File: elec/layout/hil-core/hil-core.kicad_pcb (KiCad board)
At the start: 4 copper layers, 81 parts, among them U4 10µH ±20%

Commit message: update core layout
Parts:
- added C30: 10µF ±10% 10V X5R, atopile:C0603-bd72f6, F.Cu at (175.9, 68.6)
- added C31: 10µF ±10% 10V X5R, atopile:C0603-bd72f6, F.Cu at (167.1, 55.7)
- added C32: 100nF ±10% 16V X7R, atopile:C0402-b3ef17, F.Cu at (177.6, 60.1)
- added C33: 100nF ±10% 16V X7R, atopile:C0402-b3ef17, F.Cu at (171.4, 68.7)
- added C34: 100nF ±10% 16V X7R, atopile:C0402-b3ef17, F.Cu at (177.5, 58.1)
- added C35: 100nF ±10% 16V X7R, atopile:C0402-b3ef17, F.Cu at (170.4, 68.7)
- added C36: 100nF ±10% 16V X7R, atopile:C0402-b3ef17, F.Cu at (173.1, 68.5)
- added C37: 100nF ±10% 16V X7R, atopile:C0402-b3ef17, F.Cu at (177.6, 63.3)
- added C38: 20pF ±5% 50V C0G, atopile:C0402-b3ef17, F.Cu at (168.5, 56.1)
- added C39: 20pF ±5% 50V C0G, atopile:C0402-b3ef17, F.Cu at (171.3, 53.9)
- added C40: 10µF ±10% 10V X5R, atopile:C0603-bd72f6, F.Cu at (166.9, 73.4)
- added C41: 10µF ±10% 10V X5R, atopile:C0603-bd72f6, F.Cu at (174.3, 71.7)
- added C42: 10µF ±10% 10V X5R, atopile:C0603-bd72f6, F.Cu at (174.4, 74.5)
- added C43: 10µF ±10% 10V X5R, atopile:C0603-bd72f6, F.Cu at (175.8, 71.7)
- added C44: 10µF ±10% 10V X5R, atopile:C0603-bd72f6, F.Cu at (172.9, 71.8)
- added C45: 10µF ±10% 10V X5R, atopile:C0603-bd72f6, F.Cu at (173.0, 74.5)
- added D10: , atopile:SOT-143_L2.9-W1.3-P1.92-LS2.3-BR-44397f, F.Cu at (167.2, 65.7)
- added D11: , atopile:SOT-143_L2.9-W1.3-P1.92-LS2.3-BR-44397f, F.Cu at (167.2, 69.0)
- added D12: , atopile:SOT-143_L2.9-W1.3-P1.92-LS2.3-BR-44397f, F.Cu at (175.3, 56.1)
- added D8: , atopile:SOT-143_L2.9-W1.3-P1.92-LS2.3-BR-44397f, F.Cu at (167.2, 59.2)
- added D9: , atopile:SOT-143_L2.9-W1.3-P1.92-LS2.3-BR-44397f, F.Cu at (167.2, 62.4)
- added R25: 33kΩ ±1% 62.5mW, atopile:R0402-56259e, F.Cu at (177.8, 62.3)
- added R26: 33kΩ ±1% 62.5mW, atopile:R0402-56259e, F.Cu at (177.8, 64.3)
- added R27: 12kΩ ±1% 62.5mW, atopile:R0402-56259e, F.Cu at (169.9, 59.0)
- added R28: 33kΩ ±1% 62.5mW, atopile:R0402-56259e, F.Cu at (177.8, 61.3)
- added R29: 33kΩ ±1% 62.5mW, atopile:R0402-56259e, F.Cu at (177.8, 59.1)
- added R30: 15kΩ ±1% 62.5mW, atopile:R0402-56259e, F.Cu at (169.1, 75.9)
- added R31: 5.1kΩ ±1% 62.5mW, atopile:R0402-56259e, F.Cu at (130.0, 56.4)
- added R32: 5.1kΩ ±1% 62.5mW, atopile:R0402-56259e, F.Cu at (130.1, 59.9)
- added U14: , atopile:SQFN-36_L6.0-W6.0-P0.50-BL-EP-5817ac, F.Cu at (172.7, 63.3)
- added U15: , atopile:SOT-23-6_L2.9-W1.6-P0.95-LS2.8-BR-bfc73b, F.Cu at (170.0, 73.7)
- added X1: , atopile:CRYSTAL-SMD_4P-L3.2-W2.5-BL-1-d85bc6, F.Cu at (171.5, 56.2)
- moved C26 8.13 mm to (163.2, 61.3)
- moved C27 8.13 mm to (163.2, 60.3)
- moved C28 8.13 mm to (163.2, 63.5)
- moved C29 8.13 mm to (163.2, 62.5)
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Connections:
- net A7 renamed line-4
- net A8 renamed usbpd.usb_connector-A8
- net DP1 renamed line-6
- net SBU1 renamed usb_connector.connector-A8
- net controller.cm5-pins[53] renamed pins[53]
- net controller.cm5-pins[89] renamed controller.cm5-pins[87]
- net controller.cm5-pins[89]-1 renamed pins[89]
- net pins[40] renamed controller.cm5.hdi_b-pins[40]
- net pins[87] renamed controller.cm5-pins[87]-1
- net usb_connector-A10 renamed A10
- net usb_connector-A11 renamed A11
- net usb_connector-B2 renamed B2
- net usb_connector-B3 renamed B3
- net usb_connector-B8 renamed B8
- net usb_connector-SSRXN1 renamed usb_connector.connector-B10
- net usb_connector-SSRXP1 renamed usb_connector.connector-B11
- net usb_connector-SSTXN1 renamed usb_connector.connector-A3
- net usb_connector-SSTXP1 renamed usb_connector.connector-A2
- net usb_uart-line renamed line-15
- net usb_uart-line-1 renamed line-10
- net usb_uart-line-2 renamed line-9
- net usb_uart-line-4 renamed line-8
- net usb_uart-line-8 renamed line-14
- net usbpd.usb_connector-A10 renamed SSRXN2
- net usbpd.usb_connector-A11 renamed SSRXP2
- net usbpd.usb_connector-B2 renamed SSTXP2
- net usbpd.usb_connector-B3 renamed SSTXN2
- net usbpd.usb_connector-B8 renamed SBU2
- net usbpd.usb_connector-SSRXN1 renamed usbpd.usb_connector-B10
- net usbpd.usb_connector-SSRXP1 renamed usbpd.usb_connector-B11
- net usbpd.usb_connector-SSTXN1 renamed usbpd.usb_connector-A3
- net usbpd.usb_connector-SSTXP1 renamed usbpd.usb_connector-A2
- C1 pad 2: gnd -> gnd-1
- C10 pad 1: hv-4 -> hv-2
- C10 pad 2: gnd -> gnd-1
- C11 pad 1: hv-4 -> hv-2
- C11 pad 2: gnd -> gnd-1
- C12 pad 1: hv-6 -> hv-9
- C12 pad 2: gnd -> gnd-1
- C15 pad 1: hv-4 -> hv-2
- C15 pad 2: gnd -> gnd-1
- C16 pad 1: hv-3 -> hv-5
- C16 pad 2: gnd -> gnd-1
- C17 pad 1: hv-5 -> hv-4
- C17 pad 2: gnd -> gnd-1
- C18 pad 1: hv-5 -> hv-4
- C18 pad 2: gnd -> gnd-1
- C19 pad 2: gnd -> gnd-1
- C2 pad 1: hv-2 -> hv
- C2 pad 2: gnd -> gnd-1
- C20 pad 1: hv-6 -> hv-9
- C20 pad 2: gnd -> gnd-1
- C21 pad 1: hv-6 -> hv-9
- C21 pad 2: gnd -> gnd-1
- C22 pad 1: gnd -> gnd-1
- C23 pad 1: gnd -> gnd-1
- C23 pad 2: usbpd.pd_controller-hv -> usbpd.pd_controller-hv-1
- C24 pad 1: gnd -> gnd-1
- C24 pad 2: usbpd.pd_controller-hv-1 -> usbpd.pd_controller-hv
- C26 pad 1: hv-1 -> hv-6
- C27 pad 1: hv-1 -> hv-6
- C28 pad 1: hv-7 -> hv-1
- C29 pad 1: hv-7 -> hv-1
- C3 pad 1: hv-2 -> hv
- C3 pad 2: gnd -> gnd-1
- C4 pad 1: hv -> hv-7
- C4 pad 2: gnd -> gnd-1
- C5 pad 1: hv -> hv-7
- C5 pad 2: gnd -> gnd-1
- C6 pad 1: hv -> hv-7
- C6 pad 2: gnd -> gnd-1
- C7 pad 2: gnd -> gnd-1
- C9 pad 1: hv -> hv-7
- C9 pad 2: gnd -> gnd-1
- CN1 pad 1: gnd -> gnd-1
- CN1 pad 100: gnd -> gnd-1
- CN1 pad 11: gnd -> gnd-1
- CN1 pad 13: controller.cm5-line-4 -> pins[25]
- CN1 pad 14: controller-line -> controller-line-14
- CN1 pad 15: pins[29] -> controller.cm5-line-4
- CN1 pad 16: gnd -> gnd-1
- CN1 pad 17: pins[33] -> controller.cm5-line
- CN1 pad 18: controller-line-4 -> controller-line-22
- CN1 pad 19: controller-line-24 -> controller-line-11
- CN1 pad 2: controller-line-34 -> controller-line-20
- CN1 pad 20: controller-line-37 -> controller-line-30
- CN1 pad 21: gnd -> gnd-1
- CN1 pad 22: controller-line-19 -> controller-line-15
- CN1 pad 23: line -> line-2
- CN1 pad 24: controller.cm5-pins[47]-1 -> controller.cm5-pins[47]
- CN1 pad 25: controller-line-17 -> line
- CN1 pad 26: gnd -> gnd-1
- CN1 pad 27: controller.cm5-pins[53]-1 -> controller.cm5-line-2
- CN1 pad 28: controller-line-5 -> controller-line-18
- CN1 pad 29: controller-line-16 -> controller-line-2
- CN1 pad 3: controller-line-23 -> controller-line-29
- CN1 pad 30: gnd -> gnd-1
- CN1 pad 33: gnd -> gnd-1
- CN1 pad 37: gnd -> gnd-1
- CN1 pad 39: hv-6 -> hv-11
- CN1 pad 4: gnd -> gnd-1
- CN1 pad 42: hv-6 -> hv-11
- CN1 pad 43: hv-6 -> hv-11
- CN1 pad 49: gnd -> gnd-1
- CN1 pad 5: controller-line-14 -> controller-line-9
- CN1 pad 57: hv-4 -> hv-2
- CN1 pad 58: hv-4 -> hv-2
- CN1 pad 59: hv-4 -> hv-2
- CN1 pad 6: controller-line-8 -> controller-line-13
- CN1 pad 60: hv-4 -> hv-2
- CN1 pad 61: hv-4 -> hv-2
- CN1 pad 62: hv-4 -> hv-2
- CN1 pad 65: gnd -> gnd-1
- CN1 pad 68: gnd -> gnd-1
- CN1 pad 7: gnd -> gnd-1
- CN1 pad 71: gnd -> gnd-1
- CN1 pad 73: controller-line-32 -> line-7
- CN1 pad 74: gnd -> gnd-1
- CN1 pad 75: controller-line-28 -> line-3
- CN1 pad 76: controller.cm5-pins[48] -> controller.cm5-pins[48]-1
- CN1 pad 77: line-1 -> line-13
- CN1 pad 79: gnd -> gnd-1
- CN1 pad 80: controller.cm5-line-2 -> controller.cm5-pins[40]
- CN1 pad 81: controller-line-10 -> controller-line-7
- CN1 pad 82: controller-line-29 -> controller-line
- CN1 pad 83: controller-line-31 -> controller-line-8
- CN1 pad 84: gnd -> gnd-1
- CN1 pad 85: controller-line-9 -> controller-line-26
- CN1 pad 86: controller-line-1 -> line-12
- CN1 pad 88: controller.cm5-line -> controller.cm5-line-5
- CN1 pad 89: gnd -> gnd-1
- CN1 pad 92: controller-line-13 -> controller-line-28
- CN1 pad 93: controller-line-2 -> controller-line-24
- CN1 pad 94: gnd -> gnd-1
- CN1 pad 95: controller-line-15 -> controller-line-16
- CN1 pad 96: controller-line-30 -> controller-line-31
- CN1 pad 97: gnd -> gnd-1
- CN1 pad 98: controller-line-7 -> controller-line-6
- CN1 pad 99: controller-line-26 -> controller-line-19
- CN2 pad 10: gnd -> gnd-1
- CN2 pad 13: gnd -> gnd-1
- CN2 pad 16: gnd -> gnd-1
- CN2 pad 17: controller-line-22 -> controller-line-5
- CN2 pad 18: controller-line-35 -> controller-line-21
- CN2 pad 19: gnd -> gnd-1
- CN2 pad 20: controller-line-33 -> controller-line-10
- CN2 pad 21: controller-line-3 -> controller-line-17
- CN2 pad 22: gnd -> gnd-1
- CN2 pad 24: controller.cm5-pins[47] -> controller.cm5-pins[47]-1
- CN2 pad 28: gnd -> gnd-1
- CN2 pad 31: gnd -> gnd-1
- CN2 pad 34: gnd -> gnd-1
- CN2 pad 37: gnd -> gnd-1
- CN2 pad 4: gnd -> gnd-1
- CN2 pad 40: gnd -> gnd-1
- CN2 pad 43: gnd -> gnd-1
- CN2 pad 46: gnd -> gnd-1
- CN2 pad 49: gnd -> gnd-1
- CN2 pad 52: gnd -> gnd-1
- CN2 pad 55: gnd -> gnd-1
- CN2 pad 58: gnd -> gnd-1
- CN2 pad 61: gnd -> gnd-1
- CN2 pad 64: gnd -> gnd-1
- CN2 pad 65: controller-line-18 -> controller-line-1
- CN2 pad 66: controller-line-6 -> controller-line-27
- CN2 pad 67: gnd -> gnd-1
- CN2 pad 69: controller-line-11 -> controller-line-4
- CN2 pad 7: gnd -> gnd-1
- CN2 pad 70: gnd -> gnd-1
- CN2 pad 71: controller-line-20 -> controller-line-23
- CN2 pad 72: controller-line-21 -> controller-line-3
- CN2 pad 73: gnd -> gnd-1
- CN2 pad 76: controller.cm5-pins[48]-1 -> controller.cm5-pins[48]
- CN2 pad 82: gnd -> gnd-1
- CN2 pad 85: gnd -> gnd-1
- CN2 pad 88: gnd -> gnd-1
- CN2 pad 91: gnd -> gnd-1
- CN2 pad 94: gnd -> gnd-1
- CN2 pad 97: gnd -> gnd-1
- CN2 pad 98: controller-line-27 -> line-5
- CN2 pad 99: controller-line-36 -> line-11
- D1 pad 1: hv -> hv-7
- D2 pad 1: controller.cm5-cathode -> controller.cm5-cathode-1
- D2 pad 2: hv-6 -> hv-11
- D3 pad 1: controller.cm5-cathode-1 -> controller.cm5-cathode
- D3 pad 2: hv-6 -> hv-11
- D4 pad 1: usbpd-line-4 -> usbpd-line
- D4 pad 2: usbpd-line-2 -> usbpd-line-5
- D4 pad 3: gnd -> gnd-1
- D5 pad 2: gnd -> gnd-1
- D6 pad 1: hv-2 -> hv
- D6 pad 2: gnd -> gnd-1
- L1 pad 1: hv-2 -> hv
- OLED1 pad 10: line-1 -> line-13
- OLED1 pad 11: line -> line-2
- OLED1 pad 14: hv-5 -> hv-4
- OLED1 pad 5: hv-3 -> hv-5
- OLED1 pad 7: gnd -> gnd-1
- OLED1 pad 8: hv-6 -> hv-9
- Q1 pad 5: hv-2 -> hv
- Q1 pad 6: hv-2 -> hv
- Q1 pad 7: hv-2 -> hv
- Q1 pad 8: hv-2 -> hv
- Q1 pad 9: hv-2 -> hv
- R1 pad 2: gnd -> gnd-1
- R10 pad 1: hv-6 -> hv-11
- R10 pad 2: controller.rj45-anode -> controller.rj45-anode-1
- R11 pad 2: gnd -> gnd-1
- R12 pad 1: hv-6 -> hv-9
- R13 pad 2: gnd -> gnd-1
- R14 pad 2: gnd -> gnd-1
- R15 pad 1: hv-3 -> hv-5
- R17 pad 1: usbpd-line-1 -> usbpd-line-2
- R18 pad 1: usbpd-line-5 -> usbpd-line-1
- R2 pad 1: hv -> hv-7
- R20 pad 2: hv-2 -> hv
- R24 pad 2: hv-7 -> hv-1
- R4 pad 2: gnd -> gnd-1
- R5 pad 2: gnd -> gnd-1
- R6 pad 1: hv-4 -> hv-2
- R7 pad 1: controller.cm5-cathode -> controller.cm5-cathode-1
- R8 pad 1: controller.cm5-cathode-1 -> controller.cm5-cathode
- R9 pad 1: hv-6 -> hv-11
- R9 pad 2: controller.rj45-anode-1 -> controller.rj45-anode
- RJ1 pad 11: controller.rj45-anode-1 -> controller.rj45-anode
- RJ1 pad 12: controller-line-2 -> controller-line-24
- RJ1 pad 13: controller-line-13 -> controller-line-28
- RJ1 pad 14: controller.rj45-anode -> controller.rj45-anode-1
- RJ1 pad P2: controller-line-8 -> controller-line-13
- RJ1 pad P3: controller-line-14 -> controller-line-9
- RJ1 pad P4: controller-line-34 -> controller-line-20
- RJ1 pad P5: controller-line-15 -> controller-line-16
- RJ1 pad P6: controller-line-30 -> controller-line-31
- RJ1 pad P7: controller-line-23 -> controller-line-29
- RJ1 pad P8: controller-line-26 -> controller-line-19
- RJ1 pad P9: controller-line-7 -> controller-line-6
- RJ1 pad SHIELD0: gnd -> gnd-1
- RJ1 pad SHIELD1: gnd -> gnd-1
- U1 pad 11: gnd -> gnd-1
- U1 pad 12: gnd -> gnd-1
- U1 pad 13: gnd -> gnd-1
- U1 pad 17: gnd -> gnd-1
- U1 pad 2: hv-2 -> hv
- U1 pad 3: hv-2 -> hv
- U1 pad 5: gnd -> gnd-1
- U1 pad 6: gnd -> gnd-1
- U10 pad 1: hv-4 -> hv-2
- U10 pad 2: gnd -> gnd-1
- U10 pad 3: hv-4 -> hv-2
- U10 pad 5: hv-6 -> hv-9
- U11 pad 1: hv-4 -> hv-2
- U11 pad 2: gnd -> gnd-1
- U11 pad 3: hv-4 -> hv-2
- U11 pad 5: hv-3 -> hv-5
- U12 pad 1: usbpd-line-4 -> usbpd-line
- U12 pad 10: gnd -> gnd-1
- U12 pad 12: gnd -> gnd-1
- U12 pad 13: gnd -> gnd-1
- U12 pad 2: usbpd-line-4 -> usbpd-line
- U12 pad 21: usbpd.pd_controller-hv -> usbpd.pd_controller-hv-1
- U12 pad 22: gnd -> gnd-1
- U12 pad 23: usbpd.pd_controller-hv-1 -> usbpd.pd_controller-hv
- U12 pad 25: gnd -> gnd-1
- U12 pad 4: usbpd-line-2 -> usbpd-line-5
- U12 pad 5: usbpd-line-2 -> usbpd-line-5
- U12 pad 6: gnd -> gnd-1
- U12 pad 7: usbpd-line-1 -> usbpd-line-2
- U12 pad 8: usbpd-line-5 -> usbpd-line-1
- U13 pad 2: usb_uart-line-6 -> line-1
- U13 pad 23: usb_uart-line-7 -> line-12
- U13 pad 24: usb_uart-line-5 -> line
- U13 pad 25: usb_uart-line-9 -> line-3
- U13 pad 26: usb_uart-line-3 -> line-7
- U13 pad 6: hv-7 -> hv-1
- U13 pad 7: hv-1 -> hv-6
- U2 pad 2: gnd -> gnd-1
- U3 pad 2: gnd -> gnd-1
- U3 pad 4: hv -> hv-7
- U3 pad 5: hv -> hv-7
- U4 pad 2: hv-4 -> hv-2
- U5 pad 3: gnd -> gnd-1
- U5 pad 5: hv-6 -> hv-11
- USB1 pad 1: gnd -> gnd-1
- USB1 pad 2: gnd -> gnd-1
- USB1 pad 3: gnd -> gnd-1
- USB1 pad 4: gnd -> gnd-1
- USB1 pad A1: gnd -> gnd-1
- USB1 pad A12: gnd -> gnd-1
- USB1 pad A5: usbpd-line-4 -> usbpd-line
- USB1 pad A6: usbpd-line -> usbpd-line-3
- USB1 pad A7: usbpd-line-3 -> usbpd-line-4
- USB1 pad B1: gnd -> gnd-1
- USB1 pad B12: gnd -> gnd-1
- USB1 pad B5: usbpd-line-2 -> usbpd-line-5
- USB1 pad B6: usbpd-line -> usbpd-line-3
- USB1 pad B7: usbpd-line-3 -> usbpd-line-4
- USB2 pad B5: B5 -> CC2
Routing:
- net gnd-1: track 14.3 -> 83.5 mm, vias 6 -> 46
- net line-4: track 0.00 -> 58.7 mm, vias 0 -> 3
- net line-12: track 0.00 -> 54.0 mm, vias 0 -> 2
- net line-6: track 0.00 -> 53.8 mm, vias 0 -> 2
- net line-7: track 0.00 -> 52.3 mm, vias 0 -> 2
- net line-3: track 0.00 -> 52.1 mm, vias 0 -> 2
- net line: track 0.00 -> 49.3 mm, vias 0 -> 2
- net hv-10: track 0.00 -> 40.8 mm, vias 0 -> 6
- net line-11: track 0.00 -> 38.7 mm, vias 0 -> 2
- net line-5: track 0.00 -> 38.1 mm, vias 0 -> 2
- net gnd: track 68.8 -> 31.2 mm, vias 40 -> 20
- net controller-line-28: track 0.00 -> 29.5 mm, vias 0 -> 1
- net controller-line-24: track 0.00 -> 24.6 mm, vias 0 -> 1
- net controller-line-2: track 24.6 -> 0.00 mm, vias 1 -> 0
- net controller-line-9: track 0.00 -> 19.6 mm, vias 0 -> 1
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- added copper zone on B.Cu, net gnd-1
- added copper zone on F.Cu, net gnd-1
- added copper zone on F.Cu, net hv-7
- removed copper zone on B.Cu, net gnd
- removed copper zone on F.Cu, net gnd
- removed copper zone on F.Cu, net hv-4
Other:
- board outline added: 1.5 x 9.6 mm

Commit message: add connectors
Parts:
- R12: value 18kΩ ±1% 62.5mW -> 10kΩ ±1% 62.5mW
- R14: value 10kΩ ±1% 62.5mW -> 3.9kΩ ±1% 62.5mW
- R15: value 24.9kΩ ±1% 62.5mW -> 10kΩ ±1% 62.5mW
- R6: value 47kΩ ±1% 62.5mW -> 10kΩ ±1% 62.5mW
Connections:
- net CC2 renamed B5
- net SW renamed buck_5v-cathode
- net controller.cm5-pins[47]-1 renamed pins[47]
- net controller.cm5-pins[87] renamed controller.cm5-pins[89]-1
- net controller.cm5-pins[87]-1 renamed pins[87]
- net controller.cm5.hdi_b-pins[23] renamed pins[23]
- net controller.cm5.hdi_b-pins[40] renamed pins[40]
- net pins[53] renamed controller.cm5-pins[53]-1
- net pins[89] renamed controller.cm5-pins[89]
- C1 pad 2: gnd-1 -> gnd
- C10 pad 1: hv-2 -> hv
- C10 pad 2: gnd-1 -> gnd
- C11 pad 1: hv-2 -> hv
- C11 pad 2: gnd-1 -> gnd
- C12 pad 1: hv-9 -> hv-2
- C12 pad 2: gnd-1 -> gnd
- C15 pad 1: hv-2 -> hv
- C15 pad 2: gnd-1 -> gnd
- C16 pad 2: gnd-1 -> gnd
- C17 pad 1: hv-4 -> hv-8
- C17 pad 2: gnd-1 -> gnd
- C18 pad 1: hv-4 -> hv-8
- C18 pad 2: gnd-1 -> gnd
- C19 pad 2: gnd-1 -> gnd
- C2 pad 1: hv -> hv-1
- C2 pad 2: gnd-1 -> gnd
- C20 pad 1: hv-9 -> hv-2
- C20 pad 2: gnd-1 -> gnd
- C21 pad 1: hv-9 -> hv-2
- C21 pad 2: gnd-1 -> gnd
- C22 pad 1: gnd-1 -> gnd
- C23 pad 1: gnd-1 -> gnd
- C24 pad 1: gnd-1 -> gnd
- C26 pad 1: hv-6 -> hv-9
- C26 pad 2: gnd-1 -> gnd
- C27 pad 1: hv-6 -> hv-9
- C27 pad 2: gnd-1 -> gnd
- C28 pad 1: hv-1 -> hv-3
- C28 pad 2: gnd-1 -> gnd
- C29 pad 1: hv-1 -> hv-3
- C29 pad 2: gnd-1 -> gnd
- C3 pad 1: hv -> hv-1
- C3 pad 2: gnd-1 -> gnd
- C30 pad 1: hv-8 -> hv-2
- C31 pad 1: hv-8 -> hv-2
- C32 pad 1: hv-8 -> hv-2
- C33 pad 1: hv-8 -> hv-2
- C34 pad 1: hv-8 -> hv-2
- C35 pad 1: hv-8 -> hv-2
- C36 pad 1: hv-8 -> hv-2
- C37 pad 1: hv-8 -> hv-2
- C4 pad 1: hv-7 -> hv-6
- C4 pad 2: gnd-1 -> gnd
- C40 pad 1: hv-3 -> hv
- C41 pad 1: hv-10 -> hv-7
- C42 pad 1: hv-10 -> hv-7
- C43 pad 1: hv-10 -> hv-7
- C44 pad 1: hv-10 -> hv-7
- C45 pad 1: hv-10 -> hv-7
- C5 pad 1: hv-7 -> hv-6
- C5 pad 2: gnd-1 -> gnd
- C6 pad 1: hv-7 -> hv-6
- C6 pad 2: gnd-1 -> gnd
- C7 pad 2: gnd-1 -> gnd
- C9 pad 1: hv-7 -> hv-6
- C9 pad 2: gnd-1 -> gnd
- CN1 pad 1: gnd-1 -> gnd
- CN1 pad 100: gnd-1 -> gnd
- CN1 pad 11: gnd-1 -> gnd
- CN1 pad 12: controller.cm5-pins[23] -> controller.cm5-line-2
- CN1 pad 13: pins[25] -> controller.cm5-line-5
- CN1 pad 14: controller-line-14 -> controller-line-5
- CN1 pad 15: controller.cm5-line-4 -> pins[29]
- CN1 pad 16: gnd-1 -> gnd
- CN1 pad 17: controller.cm5-line -> pins[33]
- CN1 pad 18: controller-line-22 -> controller-line-10
- CN1 pad 19: controller-line-11 -> controller-line-14
- CN1 pad 2: controller-line-20 -> controller-line-19
- CN1 pad 20: controller-line-30 -> controller-line-29
- CN1 pad 21: gnd-1 -> gnd
- CN1 pad 22: controller-line-15 -> controller-line-9
- CN1 pad 23: line-2 -> line-5
- CN1 pad 24: controller.cm5-pins[47] -> controller.cm5-line-1
- CN1 pad 25: line -> line-11
- CN1 pad 26: gnd-1 -> gnd
- CN1 pad 27: controller.cm5-line-2 -> controller.cm5-pins[53]
- CN1 pad 28: controller-line-18 -> controller-line-24
- CN1 pad 29: controller-line-2 -> controller-line-1
- CN1 pad 3: controller-line-29 -> controller-line-11
- CN1 pad 30: gnd-1 -> gnd
- CN1 pad 33: gnd-1 -> gnd
- CN1 pad 37: gnd-1 -> gnd
- CN1 pad 39: hv-11 -> hv-4
- CN1 pad 4: gnd-1 -> gnd
- CN1 pad 42: hv-11 -> hv-4
- CN1 pad 43: hv-11 -> hv-4
- CN1 pad 49: gnd-1 -> gnd
- CN1 pad 5: controller-line-9 -> controller-line-20
- CN1 pad 57: hv-2 -> hv
- CN1 pad 58: hv-2 -> hv
- CN1 pad 59: hv-2 -> hv
- CN1 pad 6: controller-line-13 -> controller-line-31
- CN1 pad 60: hv-2 -> hv
- CN1 pad 61: hv-2 -> hv
- CN1 pad 62: hv-2 -> hv
- CN1 pad 65: gnd-1 -> gnd
- CN1 pad 68: gnd-1 -> gnd
- CN1 pad 7: gnd-1 -> gnd
- CN1 pad 71: gnd-1 -> gnd
- CN1 pad 73: line-7 -> line-12
- CN1 pad 74: gnd-1 -> gnd
- CN1 pad 75: line-3 -> line-15
- CN1 pad 77: line-13 -> line-7
- CN1 pad 78: controller.cm5-pins[44] -> controller.cm5-pins[44]-1
- CN1 pad 79: gnd-1 -> gnd
- CN1 pad 80: controller.cm5-pins[40] -> controller.cm5-line-4
- CN1 pad 81: controller-line-7 -> controller-line-3
- CN1 pad 82: controller-line -> controller-line-27
- CN1 pad 83: controller-line-8 -> controller-line-4
- CN1 pad 84: gnd-1 -> gnd
- CN1 pad 86: line-12 -> line-10
- CN1 pad 87: controller.cm5-line-1 -> controller.cm5-line
- CN1 pad 88: controller.cm5-line-5 -> pins[24]
- CN1 pad 89: gnd-1 -> gnd
- CN1 pad 92: controller-line-28 -> controller-line-30
- CN1 pad 93: controller-line-24 -> controller-line-13
- CN1 pad 94: gnd-1 -> gnd
- CN1 pad 95: controller-line-16 -> controller-line-28
- CN1 pad 96: controller-line-31 -> controller-line-21
- CN1 pad 97: gnd-1 -> gnd
- CN1 pad 98: controller-line-6 -> controller-line-25
- CN1 pad 99: controller-line-19 -> controller-line-17
- CN2 pad 10: gnd-1 -> gnd
- CN2 pad 13: gnd-1 -> gnd
- CN2 pad 15: controller-line-25 -> controller-line-2
- CN2 pad 16: gnd-1 -> gnd
- CN2 pad 17: controller-line-5 -> controller-line-18
- CN2 pad 18: controller-line-21 -> controller-line-22
- CN2 pad 19: gnd-1 -> gnd
- CN2 pad 20: controller-line-10 -> controller-line-12
- CN2 pad 21: controller-line-17 -> controller-line-15
- CN2 pad 22: gnd-1 -> gnd
- CN2 pad 28: gnd-1 -> gnd
- CN2 pad 31: gnd-1 -> gnd
- CN2 pad 34: gnd-1 -> gnd
- CN2 pad 37: gnd-1 -> gnd
- CN2 pad 4: gnd-1 -> gnd
- CN2 pad 40: gnd-1 -> gnd
- CN2 pad 43: gnd-1 -> gnd
- CN2 pad 46: gnd-1 -> gnd
- CN2 pad 49: gnd-1 -> gnd
- CN2 pad 52: gnd-1 -> gnd
- CN2 pad 55: gnd-1 -> gnd
- CN2 pad 58: gnd-1 -> gnd
- CN2 pad 61: gnd-1 -> gnd
- CN2 pad 64: gnd-1 -> gnd
- CN2 pad 65: controller-line-1 -> controller-line-7
- CN2 pad 66: controller-line-27 -> controller-line-8
- CN2 pad 67: gnd-1 -> gnd
- CN2 pad 68: controller-line-12 -> controller-line-6
- CN2 pad 69: controller-line-4 -> controller-line-16
- CN2 pad 7: gnd-1 -> gnd
- CN2 pad 70: gnd-1 -> gnd
- CN2 pad 71: controller-line-23 -> controller-line
- CN2 pad 72: controller-line-3 -> controller-line-23
- CN2 pad 73: gnd-1 -> gnd
- CN2 pad 78: controller.cm5-pins[44]-1 -> controller.cm5-pins[44]
- CN2 pad 82: gnd-1 -> gnd
- CN2 pad 85: gnd-1 -> gnd
- CN2 pad 88: gnd-1 -> gnd
- CN2 pad 91: gnd-1 -> gnd
- CN2 pad 94: gnd-1 -> gnd
- CN2 pad 97: gnd-1 -> gnd
- CN2 pad 98: line-5 -> line-2
- CN2 pad 99: line-11 -> line-6
- D1 pad 1: hv-7 -> hv-6
- D10 pad 2: usb_hub-line-3 -> usb_hub-line-2
- D10 pad 3: usb_hub-line-4 -> usb_hub-line-3
- D10 pad 4: hv-10 -> hv-7
- D11 pad 2: usb_hub-line -> usb_hub-line-4
- D11 pad 3: usb_hub-line-2 -> usb_hub-line
- D11 pad 4: hv-10 -> hv-7
- D12 pad 2: line-4 -> line-9
- D12 pad 3: line-6 -> line-8
- D12 pad 4: hv-10 -> hv-7
- D2 pad 2: hv-11 -> hv-4
- D3 pad 2: hv-11 -> hv-4
- D4 pad 1: usbpd-line -> usbpd-line-3
- D4 pad 2: usbpd-line-5 -> usbpd-line-4
- D4 pad 3: gnd-1 -> gnd
- D5 pad 2: gnd-1 -> gnd
- D6 pad 1: hv -> hv-1
- D6 pad 2: gnd-1 -> gnd
- D7 pad 1: gnd-1 -> gnd
- D7 pad 2: line-15 -> line-14
- D7 pad 3: line-8 -> line
- D8 pad 2: line-15 -> line-14
- D8 pad 3: line-8 -> line
- D8 pad 4: hv-10 -> hv-7
- D9 pad 2: line-11 -> line-6
- D9 pad 3: line-5 -> line-2
- D9 pad 4: hv-10 -> hv-7
- L1 pad 1: hv -> hv-1
- OLED1 pad 10: line-13 -> line-7
- OLED1 pad 11: line-2 -> line-5
- OLED1 pad 14: hv-4 -> hv-8
- OLED1 pad 7: gnd-1 -> gnd
- OLED1 pad 8: hv-9 -> hv-2
- Q1 pad 5: hv -> hv-1
- Q1 pad 6: hv -> hv-1
- Q1 pad 7: hv -> hv-1
- Q1 pad 8: hv -> hv-1
- Q1 pad 9: hv -> hv-1
- R1 pad 2: gnd-1 -> gnd
- R10 pad 1: hv-11 -> hv-4
- R11 pad 2: gnd-1 -> gnd
- R12 pad 1: hv-9 -> hv-2
- R13 pad 2: gnd-1 -> gnd
- R14 pad 2: gnd-1 -> gnd
- R17 pad 1: usbpd-line-2 -> usbpd-line-1
- R18 pad 1: usbpd-line-1 -> usbpd-line-2
- R2 pad 1: hv-7 -> hv-6
- R20 pad 2: hv -> hv-1
- R23 pad 2: gnd-1 -> gnd
- R24 pad 2: hv-1 -> hv-3
- R31 pad 2: usb_connector-gnd -> gnd
- R32 pad 2: usb_connector-gnd -> gnd
- R4 pad 2: gnd-1 -> gnd
- R5 pad 2: gnd-1 -> gnd
- R6 pad 1: hv-2 -> hv
- R9 pad 1: hv-11 -> hv-4
- RJ1 pad 12: controller-line-24 -> controller-line-13
- RJ1 pad 13: controller-line-28 -> controller-line-30
- RJ1 pad P2: controller-line-13 -> controller-line-31
- RJ1 pad P3: controller-line-9 -> controller-line-20
- RJ1 pad P4: controller-line-20 -> controller-line-19
- RJ1 pad P5: controller-line-16 -> controller-line-28
- RJ1 pad P6: controller-line-31 -> controller-line-21
- RJ1 pad P7: controller-line-29 -> controller-line-11
- RJ1 pad P8: controller-line-19 -> controller-line-17
- RJ1 pad P9: controller-line-6 -> controller-line-25
- RJ1 pad SHIELD0: gnd-1 -> gnd
- RJ1 pad SHIELD1: gnd-1 -> gnd
- U1 pad 11: gnd-1 -> gnd
- U1 pad 12: gnd-1 -> gnd
- U1 pad 13: gnd-1 -> gnd
- U1 pad 17: gnd-1 -> gnd
- U1 pad 2: hv -> hv-1
- U1 pad 3: hv -> hv-1
- U1 pad 5: gnd-1 -> gnd
- U1 pad 6: gnd-1 -> gnd
- U10 pad 1: hv-2 -> hv
- U10 pad 2: gnd-1 -> gnd
- U10 pad 3: hv-2 -> hv
- U10 pad 5: hv-9 -> hv-2
- U11 pad 1: hv-2 -> hv
- U11 pad 2: gnd-1 -> gnd
- U11 pad 3: hv-2 -> hv
- U12 pad 1: usbpd-line -> usbpd-line-3
- U12 pad 10: gnd-1 -> gnd
- U12 pad 12: gnd-1 -> gnd
- U12 pad 13: gnd-1 -> gnd
- U12 pad 2: usbpd-line -> usbpd-line-3
- U12 pad 22: gnd-1 -> gnd
- U12 pad 25: gnd-1 -> gnd
- U12 pad 4: usbpd-line-5 -> usbpd-line-4
- U12 pad 5: usbpd-line-5 -> usbpd-line-4
- U12 pad 6: gnd-1 -> gnd
- U12 pad 7: usbpd-line-2 -> usbpd-line-1
- U12 pad 8: usbpd-line-1 -> usbpd-line-2
- U13 pad 1: line-14 -> line-1
- U13 pad 2: line-1 -> line-3
- U13 pad 23: line-12 -> line-10
- U13 pad 24: line -> line-11
- U13 pad 25: line-3 -> line-15
- U13 pad 26: line-7 -> line-12
- U13 pad 27: line-10 -> line-13
- U13 pad 28: line-9 -> line-4
- U13 pad 29: gnd-1 -> gnd
- U13 pad 3: gnd-1 -> gnd
- U13 pad 4: line-8 -> line
- U13 pad 5: line-15 -> line-14
- U13 pad 6: hv-1 -> hv-3
- U13 pad 7: hv-6 -> hv-9
- U14 pad 1: line-15 -> line-14
- U14 pad 10: hv-8 -> hv-2
- U14 pad 15: hv-8 -> hv-2
- U14 pad 2: line-8 -> line
- U14 pad 23: hv-8 -> hv-2
- U14 pad 27: hv-8 -> hv-2
- U14 pad 29: hv-8 -> hv-2
- U14 pad 3: line-11 -> line-6
- U14 pad 30: line-4 -> line-9
- U14 pad 31: line-6 -> line-8
- U14 pad 36: hv-8 -> hv-2
- U14 pad 4: line-5 -> line-2
- U14 pad 5: hv-8 -> hv-2
- U14 pad 6: usb_hub-line-3 -> usb_hub-line-2
- U14 pad 7: usb_hub-line-4 -> usb_hub-line-3
- U14 pad 8: usb_hub-line -> usb_hub-line-4
- U14 pad 9: usb_hub-line-2 -> usb_hub-line
- U15 pad 1: hv-3 -> hv
- U15 pad 6: hv-10 -> hv-7
- U2 pad 2: gnd-1 -> gnd
- U3 pad 2: gnd-1 -> gnd
- U3 pad 4: hv-7 -> hv-6
- U3 pad 5: hv-7 -> hv-6
- U4 pad 2: hv-2 -> hv
- U5 pad 3: gnd-1 -> gnd
- U5 pad 5: hv-11 -> hv-4
- USB1 pad 1: gnd-1 -> gnd
- USB1 pad 2: gnd-1 -> gnd
- USB1 pad 3: gnd-1 -> gnd
- USB1 pad 4: gnd-1 -> gnd
- USB1 pad A1: gnd-1 -> gnd
- USB1 pad A10: SSRXN2 -> A10
- USB1 pad A11: SSRXP2 -> A11
- USB1 pad A12: gnd-1 -> gnd
- USB1 pad A5: usbpd-line -> usbpd-line-3
- USB1 pad A6: usbpd-line-3 -> usbpd-line-5
- USB1 pad A7: usbpd-line-4 -> usbpd-line
- USB1 pad B1: gnd-1 -> gnd
- USB1 pad B12: gnd-1 -> gnd
- USB1 pad B2: SSTXP2 -> B2
- USB1 pad B3: SSTXN2 -> B3
- USB1 pad B5: usbpd-line-5 -> usbpd-line-4
- USB1 pad B6: usbpd-line-3 -> usbpd-line-5
- USB1 pad B7: usbpd-line-4 -> usbpd-line
- USB1 pad B8: SBU2 -> B8
- USB2 pad 1: usb_connector-gnd -> gnd
- USB2 pad 2: usb_connector-gnd -> gnd
- USB2 pad 3: usb_connector-gnd -> gnd
- USB2 pad 4: usb_connector-gnd -> gnd
- USB2 pad A1: usb_connector-gnd -> gnd
- USB2 pad A10: A10 -> SSRXN2
- USB2 pad A11: A11 -> SSRXP2
- USB2 pad A12: usb_connector-gnd -> gnd
- USB2 pad A6: line-6 -> line-8
- USB2 pad A7: line-4 -> line-9
- USB2 pad B1: usb_connector-gnd -> gnd
- USB2 pad B12: usb_connector-gnd -> gnd
- USB2 pad B2: B2 -> SSTXP2
- USB2 pad B3: B3 -> SSTXN2
- USB2 pad B6: line-6 -> line-8
- USB2 pad B7: line-4 -> line-9
- USB2 pad B8: B8 -> SBU2
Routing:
- net gnd: track 31.2 -> 123.1 mm, vias 20 -> 66
- net gnd-1: track 83.5 -> 0.00 mm, vias 46 -> 0
- net line-9: track 0.00 -> 58.7 mm, vias 0 -> 3
- net line-4: track 58.7 -> 0.00 mm, vias 3 -> 0
- net line-10: track 0.00 -> 54.0 mm, vias 0 -> 2
- net line-7: track 52.3 -> 0.00 mm, vias 2 -> 0
- net line-3: track 52.1 -> 0.00 mm, vias 2 -> 0
- net hv-10: track 40.8 -> 0.00 mm, vias 6 -> 0
- net line-8: track 14.9 -> 53.8 mm
- net line-5: track 38.1 -> 0.00 mm, vias 2 -> 0
- net line-2: track 0.00 -> 38.1 mm, vias 0 -> 2
- net line-15: track 16.9 -> 52.1 mm
- net line: track 49.3 -> 14.9 mm
- net controller-line-30: track 0.00 -> 29.5 mm, vias 0 -> 1
- net hv-7: track 14.5 -> 40.8 mm, vias 12 -> 6
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- added copper zone on B.Cu, net (none)
- added copper zone on F.Cu, net (none)
- added copper zone on F.Cu, net hv-1
- added copper zone on F.Cu, net hv-6
- removed copper zone on B.Cu, net gnd-1
- removed copper zone on F.Cu, net gnd-1
- removed copper zone on F.Cu, net hv-2
- removed copper zone on F.Cu, net hv-7
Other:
- board outline removed

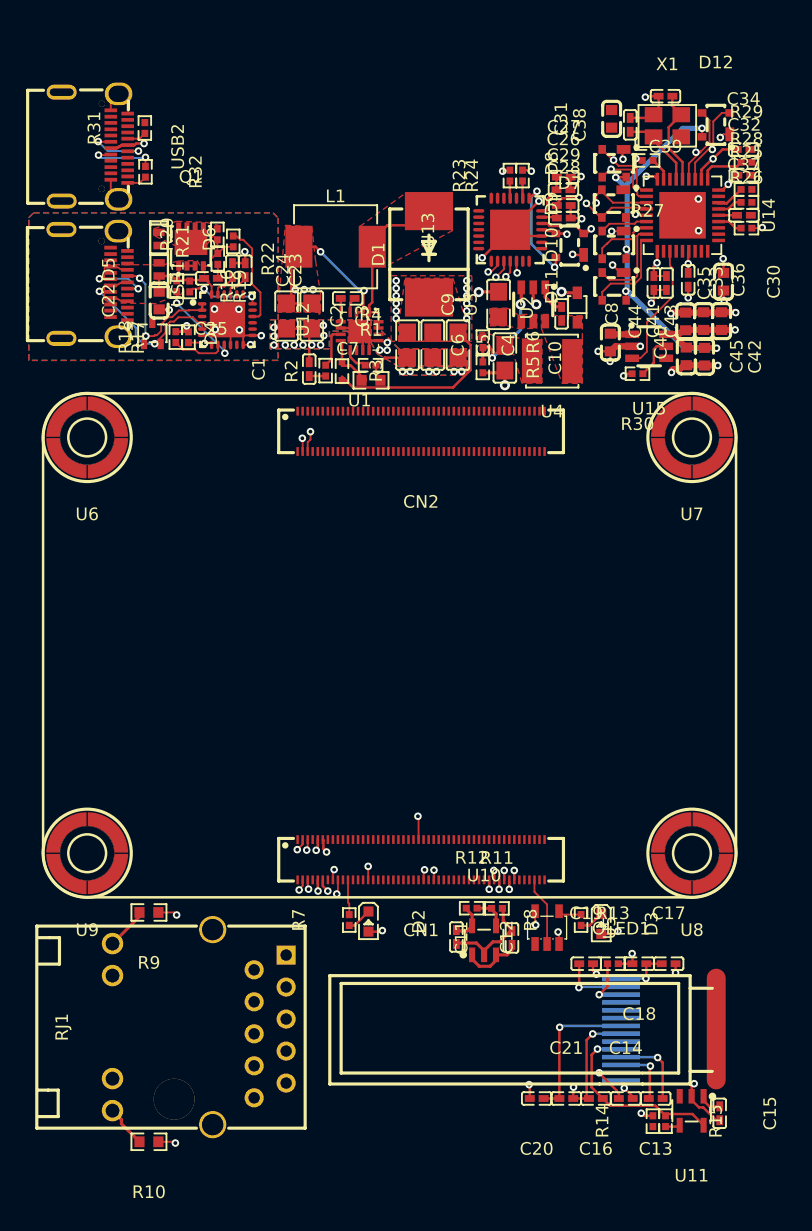
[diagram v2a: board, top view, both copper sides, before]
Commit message: update layouts to kicad 9
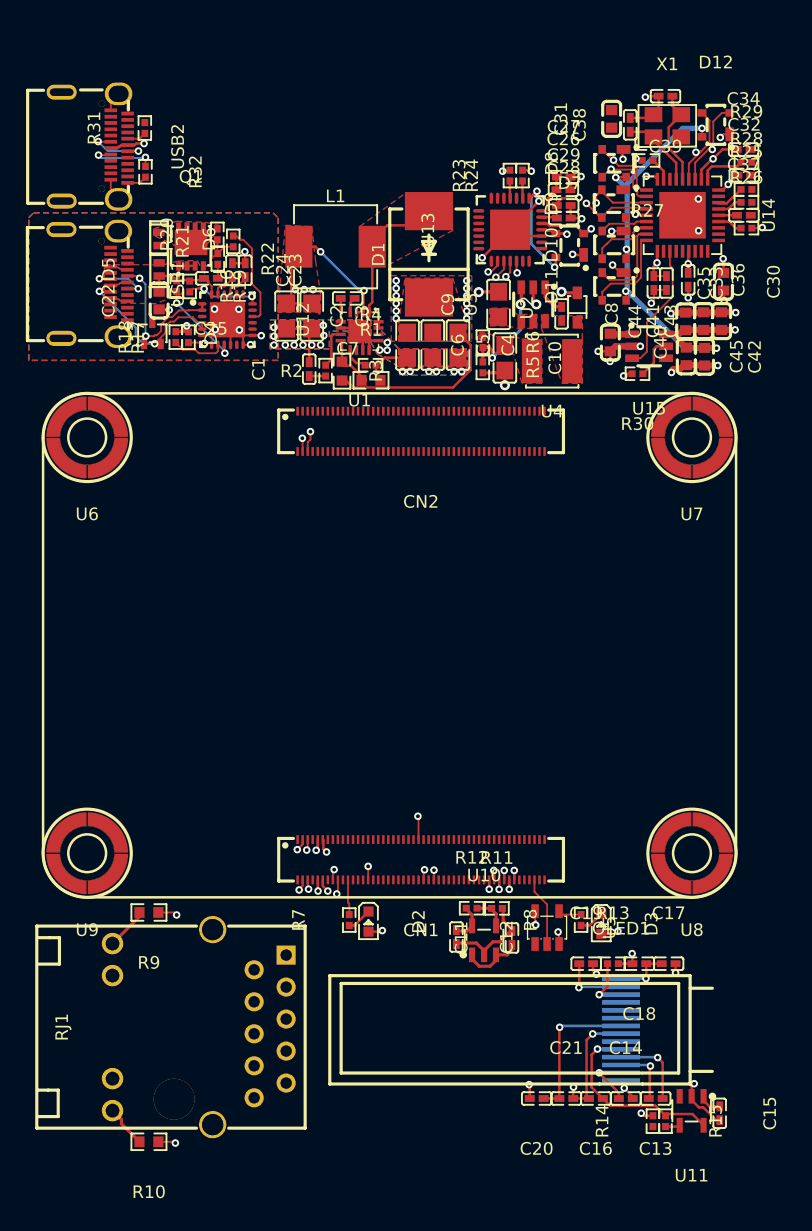
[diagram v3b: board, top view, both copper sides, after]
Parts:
- R2: value 180kΩ ±1% 62.5mW -> 180kΩ ±1% 100mW; footprint atopile:R0402-56259e -> atopile:R0603-ebcab9
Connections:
- net A10 renamed usbpd.usb_connector-A10
- net A11 renamed usbpd.usb_connector-A11
- net B2 renamed usbpd.usb_connector-B2
- net B3 renamed usbpd.usb_connector-B3
- net B5 renamed CC2
- net B8 renamed usbpd.usb_connector-B8
- net SBU2 renamed usb_connector.connector-B8
- net SSRXN2 renamed usb_connector.connector-A10
- net SSRXP2 renamed usb_connector.connector-A11
- net SSTXN2 renamed usb_connector.connector-B3
- net SSTXP2 renamed usb_connector.connector-B2
- net buck_5v-cathode renamed SW
- net controller.cm5-pins[44] renamed pins[44]
- net controller.cm5-pins[48] renamed pins[48]
- net controller.cm5-pins[53]-1 renamed pins[53]
- net controller.cm5-pins[89] renamed pins[89]
- net controller.cm5-pins[89]-1 renamed controller.cm5-pins[87]
- net line-13 renamed usb_uart-line-1
- net pins[26] renamed controller.cm5.hdi_b-pins[26]
- net pins[47] renamed controller.cm5-pins[47]
- net pins[87] renamed controller.cm5-pins[87]-1
- C10 pad 1: hv -> hv-8
- C11 pad 1: hv -> hv-8
- C12 pad 1: hv-2 -> hv
- C15 pad 1: hv -> hv-8
- C16 pad 1: hv-5 -> hv-1
- C17 pad 1: hv-8 -> hv-6
- C18 pad 1: hv-8 -> hv-6
- C2 pad 1: hv-1 -> hv-7
- C20 pad 1: hv-2 -> hv
- C21 pad 1: hv-2 -> hv
- C23 pad 2: usbpd.pd_controller-hv-1 -> usbpd.pd_controller-hv
- C24 pad 2: usbpd.pd_controller-hv -> usbpd.pd_controller-hv-1
- C26 pad 1: hv-9 -> hv-2
- C26 pad 2: gnd -> gnd-1
- C27 pad 1: hv-9 -> hv-2
- C27 pad 2: gnd -> gnd-1
- C28 pad 2: gnd -> gnd-1
- C29 pad 2: gnd -> gnd-1
- C3 pad 1: hv-1 -> hv-7
- C30 pad 1: hv-2 -> hv
- C31 pad 1: hv-2 -> hv
- C32 pad 1: hv-2 -> hv
- C33 pad 1: hv-2 -> hv
- C34 pad 1: hv-2 -> hv
- C35 pad 1: hv-2 -> hv
- C36 pad 1: hv-2 -> hv
- C37 pad 1: hv-2 -> hv
- C4 pad 1: hv-6 -> hv-4
- C40 pad 1: hv -> hv-8
- C41 pad 1: hv-7 -> hv-5
- C42 pad 1: hv-7 -> hv-5
- C43 pad 1: hv-7 -> hv-5
- C44 pad 1: hv-7 -> hv-5
- C45 pad 1: hv-7 -> hv-5
- C5 pad 1: hv-6 -> hv-4
- C6 pad 1: hv-6 -> hv-4
- C9 pad 1: hv-6 -> hv-4
- CN1 pad 12: controller.cm5-line-2 -> controller.cm5-line-4
- CN1 pad 13: controller.cm5-line-5 -> pins[25]
- CN1 pad 14: controller-line-5 -> controller-line-3
- CN1 pad 15: pins[29] -> controller.cm5-line
- CN1 pad 18: controller-line-10 -> controller-line-12
- CN1 pad 19: controller-line-14 -> controller-line-11
- CN1 pad 2: controller-line-19 -> controller-line-24
- CN1 pad 20: controller-line-29 -> controller-line-9
- CN1 pad 22: controller-line-9 -> controller-line-10
- CN1 pad 23: line-5 -> line-4
- CN1 pad 24: controller.cm5-line-1 -> controller.cm5-pins[47]-1
- CN1 pad 25: line-11 -> line
- CN1 pad 27: controller.cm5-pins[53] -> controller.cm5-line-1
- CN1 pad 28: controller-line-24 -> controller-line-26
- CN1 pad 29: controller-line-1 -> controller-line-16
- CN1 pad 3: controller-line-11 -> controller-line-4
- CN1 pad 39: hv-4 -> hv-9
- CN1 pad 42: hv-4 -> hv-9
- CN1 pad 43: hv-4 -> hv-9
- CN1 pad 5: controller-line-20 -> controller-line-2
- CN1 pad 57: hv -> hv-8
- CN1 pad 58: hv -> hv-8
- CN1 pad 59: hv -> hv-8
- CN1 pad 6: controller-line-31 -> controller-line-21
- CN1 pad 60: hv -> hv-8
- CN1 pad 61: hv -> hv-8
- CN1 pad 62: hv -> hv-8
- CN1 pad 73: line-12 -> line-6
- CN1 pad 75: line-15 -> line-10
- CN1 pad 76: controller.cm5-pins[48]-1 -> controller.cm5-line-3
- CN1 pad 77: line-7 -> line-3
- CN1 pad 78: controller.cm5-pins[44]-1 -> controller.cm5-line-5
- CN1 pad 80: controller.cm5-line-4 -> controller.cm5-line-2
- CN1 pad 81: controller-line-3 -> controller-line
- CN1 pad 82: controller-line-27 -> controller-line-7
- CN1 pad 83: controller-line-4 -> controller-line-5
- CN1 pad 85: controller-line-26 -> controller-line-8
- CN1 pad 86: line-10 -> line-9
- CN1 pad 87: controller.cm5-line -> controller.cm5-pins[26]
- CN1 pad 92: controller-line-30 -> controller-line-28
- CN1 pad 93: controller-line-13 -> controller-line-19
- CN1 pad 95: controller-line-28 -> controller-line-27
- CN1 pad 96: controller-line-21 -> controller-line-15
- CN1 pad 98: controller-line-25 -> controller-line-30
- CN1 pad 99: controller-line-17 -> controller-line-31
- CN2 pad 15: controller-line-2 -> controller-line-23
- CN2 pad 17: controller-line-18 -> controller-line-17
- CN2 pad 18: controller-line-22 -> controller-line-20
- CN2 pad 20: controller-line-12 -> controller-line-1
- CN2 pad 21: controller-line-15 -> controller-line-6
- CN2 pad 65: controller-line-7 -> controller-line-22
- CN2 pad 66: controller-line-8 -> controller-line-25
- CN2 pad 68: controller-line-6 -> controller-line-13
- CN2 pad 69: controller-line-16 -> controller-line-18
- CN2 pad 71: controller-line -> controller-line-29
- CN2 pad 72: controller-line-23 -> controller-line-14
- CN2 pad 99: line-6 -> line-1
- D1 pad 1: hv-6 -> hv-4
- D10 pad 3: usb_hub-line-3 -> usb_hub-line-1
- D10 pad 4: hv-7 -> hv-5
- D11 pad 2: usb_hub-line-4 -> usb_hub-line
- D11 pad 3: usb_hub-line -> usb_hub-line-4
- D11 pad 4: hv-7 -> hv-5
- D12 pad 2: line-9 -> line-8
- D12 pad 3: line-8 -> line-7
- D12 pad 4: hv-7 -> hv-5
- D2 pad 2: hv-4 -> hv-9
- D3 pad 2: hv-4 -> hv-9
- D4 pad 1: usbpd-line-3 -> usbpd-line-5
- D4 pad 2: usbpd-line-4 -> usbpd-line-3
- D6 pad 1: hv-1 -> hv-7
- D7 pad 1: gnd -> gnd-1
- D7 pad 2: line-14 -> line-11
- D7 pad 3: line -> line-5
- D8 pad 2: line-14 -> line-11
- D8 pad 3: line -> line-5
- D8 pad 4: hv-7 -> hv-5
- D9 pad 2: line-6 -> line-1
- D9 pad 4: hv-7 -> hv-5
- L1 pad 1: hv-1 -> hv-7
- OLED1 pad 10: line-7 -> line-3
- OLED1 pad 11: line-5 -> line-4
- OLED1 pad 14: hv-8 -> hv-6
- OLED1 pad 5: hv-5 -> hv-1
- OLED1 pad 8: hv-2 -> hv
- Q1 pad 5: hv-1 -> hv-7
- Q1 pad 6: hv-1 -> hv-7
- Q1 pad 7: hv-1 -> hv-7
- Q1 pad 8: hv-1 -> hv-7
- Q1 pad 9: hv-1 -> hv-7
- R10 pad 1: hv-4 -> hv-9
- R10 pad 2: controller.rj45-anode-1 -> controller.rj45-anode
- R12 pad 1: hv-2 -> hv
- R15 pad 1: hv-5 -> hv-1
- R17 pad 1: usbpd-line-1 -> usbpd-line-4
- R18 pad 1: usbpd-line-2 -> usbpd-line
- R2 pad 1: hv-6 -> hv-4
- R20 pad 2: hv-1 -> hv-7
- R23 pad 2: gnd -> gnd-1
- R6 pad 1: hv -> hv-8
- R8 pad 2: controller.cm5-line-3 -> Y
- R9 pad 1: hv-4 -> hv-9
- R9 pad 2: controller.rj45-anode -> controller.rj45-anode-1
- RJ1 pad 11: controller.rj45-anode -> controller.rj45-anode-1
- RJ1 pad 12: controller-line-13 -> controller-line-19
- RJ1 pad 13: controller-line-30 -> controller-line-28
- RJ1 pad 14: controller.rj45-anode-1 -> controller.rj45-anode
- RJ1 pad P1: controller.rj45.connector-net-1 -> controller.rj45.connector-net
- RJ1 pad P10: controller.rj45.connector-net -> controller.rj45.connector-net-1
- RJ1 pad P2: controller-line-31 -> controller-line-21
- RJ1 pad P3: controller-line-20 -> controller-line-2
- RJ1 pad P4: controller-line-19 -> controller-line-24
- RJ1 pad P5: controller-line-28 -> controller-line-27
- RJ1 pad P6: controller-line-21 -> controller-line-15
- RJ1 pad P7: controller-line-11 -> controller-line-4
- RJ1 pad P8: controller-line-17 -> controller-line-31
- RJ1 pad P9: controller-line-25 -> controller-line-30
- U1 pad 2: hv-1 -> hv-7
- U1 pad 3: hv-1 -> hv-7
- U10 pad 1: hv -> hv-8
- U10 pad 3: hv -> hv-8
- U10 pad 5: hv-2 -> hv
- U11 pad 1: hv -> hv-8
- U11 pad 3: hv -> hv-8
- U11 pad 5: hv-5 -> hv-1
- U12 pad 1: usbpd-line-3 -> usbpd-line-5
- U12 pad 2: usbpd-line-3 -> usbpd-line-5
- U12 pad 21: usbpd.pd_controller-hv-1 -> usbpd.pd_controller-hv
- U12 pad 23: usbpd.pd_controller-hv -> usbpd.pd_controller-hv-1
- U12 pad 4: usbpd-line-4 -> usbpd-line-3
- U12 pad 5: usbpd-line-4 -> usbpd-line-3
- U12 pad 7: usbpd-line-1 -> usbpd-line-4
- U12 pad 8: usbpd-line-2 -> usbpd-line
- U13 pad 1: line-1 -> usb_uart-line-3
- U13 pad 2: line-3 -> usb_uart-line
- U13 pad 23: line-10 -> line
- U13 pad 24: line-11 -> line-9
- U13 pad 25: line-15 -> line-6
- U13 pad 26: line-12 -> line-10
- U13 pad 28: line-4 -> usb_uart-line-2
- U13 pad 29: gnd -> gnd-1
- U13 pad 3: gnd -> gnd-1
- U13 pad 4: line -> line-5
- U13 pad 5: line-14 -> line-11
- U13 pad 7: hv-9 -> hv-2
- U14 pad 1: line-14 -> line-11
- U14 pad 10: hv-2 -> hv
- U14 pad 12: usb_hub-line-1 -> usb_hub-line-3
- U14 pad 15: hv-2 -> hv
- U14 pad 2: line -> line-5
- U14 pad 23: hv-2 -> hv
- U14 pad 27: hv-2 -> hv
- U14 pad 29: hv-2 -> hv
- U14 pad 3: line-6 -> line-1
- U14 pad 30: line-9 -> line-8
- U14 pad 31: line-8 -> line-7
- U14 pad 36: hv-2 -> hv
- U14 pad 5: hv-2 -> hv
- U14 pad 7: usb_hub-line-3 -> usb_hub-line-1
- U14 pad 8: usb_hub-line-4 -> usb_hub-line
- U14 pad 9: usb_hub-line -> usb_hub-line-4
- U15 pad 1: hv -> hv-8
- U15 pad 3: usb_hub-line-1 -> usb_hub-line-3
- U15 pad 6: hv-7 -> hv-5
- U3 pad 4: hv-6 -> hv-4
- U3 pad 5: hv-6 -> hv-4
- U4 pad 2: hv -> hv-8
- U5 pad 4: controller.cm5-line-3 -> Y
- U5 pad 5: hv-4 -> hv-9
- USB1 pad A5: usbpd-line-3 -> usbpd-line-5
- USB1 pad A6: usbpd-line-5 -> usbpd-line-1
- USB1 pad A7: usbpd-line -> usbpd-line-2
- USB1 pad B5: usbpd-line-4 -> usbpd-line-3
- USB1 pad B6: usbpd-line-5 -> usbpd-line-1
- USB1 pad B7: usbpd-line -> usbpd-line-2
- USB2 pad A6: line-8 -> line-7
- USB2 pad A7: line-9 -> line-8
- USB2 pad B6: line-8 -> line-7
- USB2 pad B7: line-9 -> line-8
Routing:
- net (no net): track 0.00 -> 207.6 mm, vias 0 -> 8
- net gnd-1: track 0.00 -> 123.1 mm, vias 0 -> 66
- net gnd: track 123.1 -> 0.00 mm, vias 66 -> 0
- net line-9: track 58.7 -> 0.00 mm, vias 3 -> 0
- net line-10: track 54.0 -> 0.00 mm, vias 2 -> 0
- net line-7: track 0.00 -> 53.8 mm, vias 0 -> 2
- net line-12: track 52.3 -> 0.00 mm, vias 2 -> 0
- net line-15: track 52.1 -> 0.00 mm, vias 2 -> 0
- net line-6: track 38.7 -> 0.00 mm, vias 2 -> 0
- net line-1: track 0.00 -> 38.7 mm, vias 0 -> 2
- net line-11: track 49.3 -> 16.9 mm
- net hv-2: track 30.5 -> 3.36 mm, vias 8 -> 0
- net hv-5: track 15.4 -> 40.8 mm, vias 1 -> 6
- net controller-line-13: track 24.6 -> 0.00 mm, vias 1 -> 0
- net hv-7: track 40.8 -> 17.0 mm, vias 6 -> 5
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- added copper zone on F.Cu, net hv-4
- added copper zone on F.Cu, net hv-7
- added copper zone on F.Cu, net hv-8
- removed copper zone on F.Cu, net hv
- removed copper zone on F.Cu, net hv-1
- removed copper zone on F.Cu, net hv-6
